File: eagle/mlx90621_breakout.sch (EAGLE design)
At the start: 7 parts, among them J1 ARDUINO_R3_SHIELD

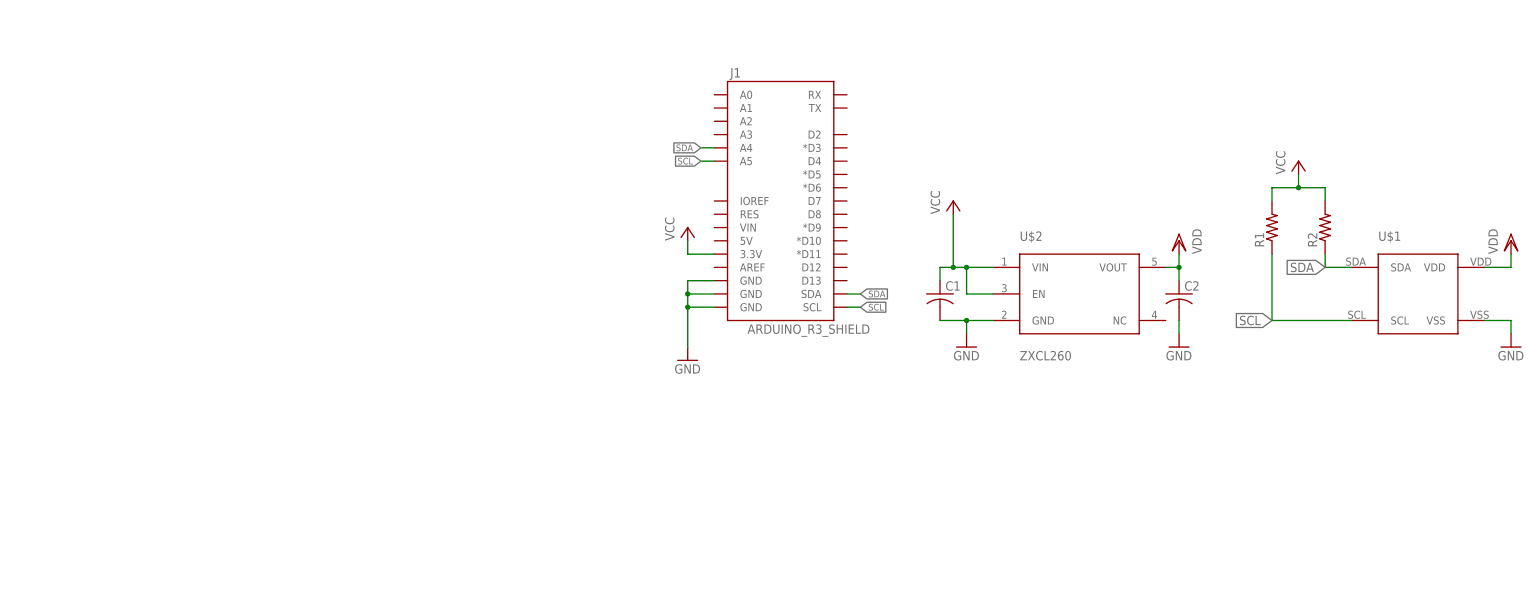
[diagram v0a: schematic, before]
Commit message: Finalizado ruteo de MLX90621 en shield (x1)
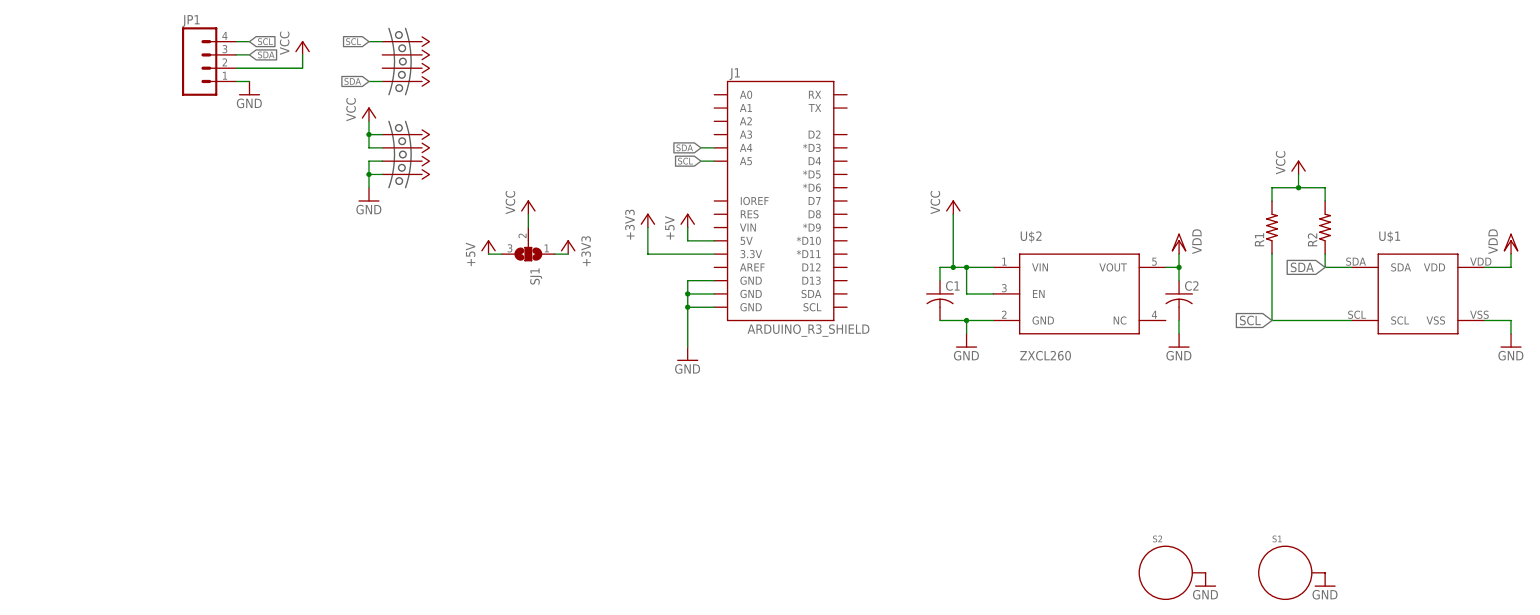
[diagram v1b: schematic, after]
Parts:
- added JP1: (no value), SparkFun-Connectors:M04PTH
- added S1, S2: STANDOFF_ELECTRICAL, SparkFun-Electromechanical:STANDOFF_ELECTRICAL
- added SJ1: (no value), jumper:SJ2W
- added U$3, U$4: MOUSE-BITES-4, mouse-bites:MOUSE-BITES-4
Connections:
- new net +3V3: J1.3.3V, SJ1.1
- new net +5V: J1.5V, SJ1.3
- net GND: now also JP1.1, S1.P$1, S2.P$1, U$4.3, U$4.4
- net SCL: now also JP1.4, U$3.1; no longer J1.SCL
- net SDA: now also JP1.3, U$3.4; no longer J1.SDA
- net VCC: now also JP1.2, SJ1.2, U$4.1, U$4.2; no longer J1.3.3V
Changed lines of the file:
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@@
 <layer number="113" name="IDFDebug" color="7" fill="1" visible="yes" active="yes"/>
 <layer number="114" name="Badge_Outline" color="11" fill="1" visible="no" active="no"/>
+<layer number="115" name="ReferenceISLANDS" color="7" fill="1" visible="yes" active="yes"/>
 <layer number="116" name="Patch_BOT" color="9" fill="4" visible="yes" active="yes"/>
 <layer number="118" name="Rect_Pads" color="7" fill="1" visible="yes" active="yes"/>
@@
 <part name="P+3" library="supply1" deviceset="VCC" device=""/>
 <part name="GND4" library="SparkFun-Aesthetics" deviceset="GND" device=""/>
+<part name="SJ1" library="jumper" deviceset="SJ2W" device=""/>
+<part name="P+4" library="supply1" deviceset="+5V" device=""/>
+<part name="P+5" library="supply1" deviceset="+5V" device=""/>
+<part name="+3V1" library="supply1" deviceset="+3V3" device=""/>
+<part name="+3V2" library="supply1" deviceset="+3V3" device=""/>
+<part name="S1" library="SparkFun-Electromechanical" deviceset="STANDOFF_ELECTRICAL" device=""/>
+<part name="S2" library="SparkFun-Electromechanical" deviceset="STANDOFF_ELECTRICAL" device=""/>
+<part name="GND5" library="SparkFun-Aesthetics" deviceset="GND" device=""/>
+<part name="GND6" library="SparkFun-Aesthetics" deviceset="GND" device=""/>
+<part name="JP1" library="SparkFun-Connectors" deviceset="M04" device="PTH"/>
+<part name="GND7" library="SparkFun-Aesthetics" deviceset="GND" device=""/>
+<part name="P+6" library="supply1" deviceset="VCC" device=""/>
+<part name="U$3" library="mouse-bites" deviceset="MOUSE-BITES-4" device=""/>
+<part name="U$4" library="mouse-bites" deviceset="MOUSE-BITES-4" device=""/>
+<part name="GND8" library="SparkFun-Aesthetics" deviceset="GND" device=""/>
+<part name="P+7" library="supply1" deviceset="VCC" device=""/>
 </parts>
 <sheets>
@@
 <instance part="VDD2" gate="G$1" x="368.3" y="76.2"/>
 <instance part="GND3" gate="1" x="368.3" y="55.88"/>
-<instance part="P+3" gate="VCC" x="210.82" y="78.74"/>
+<instance part="P+3" gate="VCC" x="180.34" y="83.82"/>
 <instance part="GND4" gate="1" x="210.82" y="53.34"/>
+<instance part="SJ1" gate="G$1" x="180.34" y="73.66" rot="R270"/>
+<instance part="P+4" gate="1" x="172.72" y="76.2"/>
+<instance part="P+5" gate="1" x="210.82" y="81.28"/>
+<instance part="+3V1" gate="G$1" x="187.96" y="76.2" rot="MR0"/>
+<instance part="+3V2" gate="G$1" x="203.2" y="81.28"/>
+<instance part="S1" gate="G$1" x="325.12" y="12.7"/>
+<instance part="S2" gate="G$1" x="302.26" y="12.7"/>
+<instance part="GND5" gate="1" x="309.88" y="10.16"/>
+<instance part="GND6" gate="1" x="332.74" y="10.16"/>
+<instance part="JP1" gate="G$1" x="119.38" y="109.22"/>
+<instance part="GND7" gate="1" x="127" y="104.14"/>
+<instance part="P+6" gate="VCC" x="137.16" y="114.3"/>
+<instance part="U$3" gate="G$1" x="152.4" y="116.84"/>
+<instance part="U$4" gate="G$1" x="152.4" y="99.06"/>
+<instance part="GND8" gate="1" x="149.86" y="83.82"/>
+<instance part="P+7" gate="VCC" x="149.86" y="101.6"/>
 </instances>
 <busses>
@@
 <wire x1="210.82" y1="68.58" x2="210.82" y2="66.04" width="0.1524" layer="91"/>
 <junction x="210.82" y="66.04"/>
+</segment>
+<segment>
+<pinref part="S2" gate="G$1" pin="P$1"/>
+<pinref part="GND5" gate="1" pin="GND"/>
+</segment>
+<segment>
+<pinref part="S1" gate="G$1" pin="P$1"/>
+<pinref part="GND6" gate="1" pin="GND"/>
+</segment>
+<segment>
+<pinref part="JP1" gate="G$1" pin="1"/>
+<wire x1="124.46" y1="106.68" x2="127" y2="106.68" width="0.1524" layer="91"/>
+<pinref part="GND7" gate="1" pin="GND"/>
+</segment>
+<segment>
+<pinref part="U$4" gate="G$1" pin="3"/>
+<wire x1="152.4" y1="91.44" x2="149.86" y2="91.44" width="0.1524" layer="91"/>
+<pinref part="U$4" gate="G$1" pin="4"/>
+<wire x1="152.4" y1="88.9" x2="149.86" y2="88.9" width="0.1524" layer="91"/>
+<wire x1="149.86" y1="91.44" x2="149.86" y2="88.9" width="0.1524" layer="91"/>
+<pinref part="GND8" gate="1" pin="GND"/>
+<wire x1="149.86" y1="88.9" x2="149.86" y2="86.36" width="0.1524" layer="91"/>
+<junction x="149.86" y="88.9"/>
 </segment>
 </net>
@@
 </segment>
 <segment>
-<pinref part="J1" gate="G$1" pin="3.3V"/>
+<pinref part="SJ1" gate="G$1" pin="2"/>
 <pinref part="P+3" gate="VCC" pin="VCC"/>
-<wire x1="215.9" y1="73.66" x2="210.82" y2="73.66" width="0.1524" layer="91"/>
-<wire x1="210.82" y1="73.66" x2="210.82" y2="76.2" width="0.1524" layer="91"/>
+<wire x1="180.34" y1="81.28" x2="180.34" y2="78.74" width="0.1524" layer="91"/>
+</segment>
+<segment>
+<pinref part="JP1" gate="G$1" pin="2"/>
+<wire x1="124.46" y1="109.22" x2="137.16" y2="109.22" width="0.1524" layer="91"/>
+<wire x1="137.16" y1="109.22" x2="137.16" y2="111.76" width="0.1524" layer="91"/>
+<pinref part="P+6" gate="VCC" pin="VCC"/>
+</segment>
+<segment>
+<pinref part="U$4" gate="G$1" pin="2"/>
+<wire x1="152.4" y1="93.98" x2="149.86" y2="93.98" width="0.1524" layer="91"/>
+<pinref part="U$4" gate="G$1" pin="1"/>
+<wire x1="152.4" y1="96.52" x2="149.86" y2="96.52" width="0.1524" layer="91"/>
+<wire x1="149.86" y1="93.98" x2="149.86" y2="96.52" width="0.1524" layer="91"/>
+<pinref part="P+7" gate="VCC" pin="VCC"/>
+<wire x1="149.86" y1="96.52" x2="149.86" y2="99.06" width="0.1524" layer="91"/>
+<junction x="149.86" y="96.52"/>
 </segment>
 </net>
@@
 </segment>
 <segment>
-<pinref part="J1" gate="G$1" pin="SDA"/>
-<wire x1="241.3" y1="66.04" x2="243.84" y2="66.04" width="0.1524" layer="91"/>
-<label x="243.84" y="66.04" size="1.27" layer="95" xref="yes"/>
-</segment>
-<segment>
 <pinref part="J1" gate="G$1" pin="A4"/>
 <wire x1="215.9" y1="93.98" x2="213.36" y2="93.98" width="0.1524" layer="91"/>
 <label x="213.36" y="93.98" size="1.27" layer="95" rot="R180" xref="yes"/>
+</segment>
+<segment>
+<pinref part="JP1" gate="G$1" pin="3"/>
+<wire x1="124.46" y1="111.76" x2="127" y2="111.76" width="0.1524" layer="91"/>
+<label x="127" y="111.76" size="1.27" layer="95" xref="yes"/>
+</segment>
+<segment>
+<pinref part="U$3" gate="G$1" pin="4"/>
+<wire x1="152.4" y1="106.68" x2="149.86" y2="106.68" width="0.1524" layer="91"/>
+<label x="149.86" y="106.68" size="1.27" layer="95" rot="R180" xref="yes"/>
 </segment>
 </net>
@@
 </segment>
 <segment>
-<pinref part="J1" gate="G$1" pin="SCL"/>
-<wire x1="241.3" y1="63.5" x2="243.84" y2="63.5" width="0.1524" layer="91"/>
-<label x="243.84" y="63.5" size="1.27" layer="95" xref="yes"/>
-</segment>
-<segment>
 <pinref part="J1" gate="G$1" pin="A5"/>
 <wire x1="215.9" y1="91.44" x2="213.36" y2="91.44" width="0.1524" layer="91"/>
 <label x="213.36" y="91.44" size="1.27" layer="95" rot="R180" xref="yes"/>
 </segment>
-</net>
+<segment>
+<pinref part="JP1" gate="G$1" pin="4"/>
+<wire x1="124.46" y1="114.3" x2="127" y2="114.3" width="0.1524" layer="91"/>
+<label x="127" y="114.3" size="1.27" layer="95" xref="yes"/>
+</segment>
+<segment>
+<pinref part="U$3" gate="G$1" pin="1"/>
+<wire x1="152.4" y1="114.3" x2="149.86" y2="114.3" width="0.1524" layer="91"/>
+<label x="149.86" y="114.3" size="1.27" layer="95" rot="R180" xref="yes"/>
+</segment>
+</net>
+<net name="+3V3" class="0">
+<segment>
+<pinref part="J1" gate="G$1" pin="3.3V"/>
+<pinref part="+3V2" gate="G$1" pin="+3V3"/>
+<wire x1="203.2" y1="78.74" x2="203.2" y2="73.66" width="0.1524" layer="91"/>
+<wire x1="203.2" y1="73.66" x2="215.9" y2="73.66" width="0.1524" layer="91"/>
+</segment>
+<segment>
+<pinref part="SJ1" gate="G$1" pin="1"/>
+<pinref part="+3V1" gate="G$1" pin="+3V3"/>
+<wire x1="187.96" y1="73.66" x2="185.42" y2="73.66" width="0.1524" layer="91"/>
+</segment>
+</net>
+<net name="+5V" class="0">
+<segment>
+<pinref part="SJ1" gate="G$1" pin="3"/>
+<pinref part="P+4" gate="1" pin="+5V"/>
+<wire x1="172.72" y1="73.66" x2="175.26" y2="73.66" width="0.1524" layer="91"/>
+</segment>
+<segment>
+<pinref part="J1" gate="G$1" pin="5V"/>
+<pinref part="P+5" gate="1" pin="+5V"/>
+<wire x1="210.82" y1="78.74" x2="210.82" y2="76.2" width="0.1524" layer="91"/>
+<wire x1="210.82" y1="76.2" x2="215.9" y2="76.2" width="0.1524" layer="91"/>
+</segment>
+</net>

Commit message: Finalizado diseño de panel shield
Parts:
- added U$5, U$6, U$7: MOUSE-BITES-4, mouse-bites:MOUSE-BITES-4
- C1, C2: value (none) -> 100n
- R1, R2: value (none) -> 10k
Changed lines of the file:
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@@
 <part name="J1" library="SparkFun-Boards" deviceset="ARDUINO_R3_SHIELD" device=""/>
 <part name="FRAME1" library="frames" deviceset="A3L-LOC" device=""/>
-<part name="C1" library="adafruit" deviceset="C-US" device="C0603"/>
-<part name="C2" library="adafruit" deviceset="C-US" device="C0603"/>
-<part name="R1" library="adafruit" deviceset="R-US_" device="R0603"/>
-<part name="R2" library="adafruit" deviceset="R-US_" device="R0603"/>
+<part name="C1" library="adafruit" deviceset="C-US" device="C0603" value="100n"/>
+<part name="C2" library="adafruit" deviceset="C-US" device="C0603" value="100n"/>
+<part name="R1" library="adafruit" deviceset="R-US_" device="R0603" value="10k"/>
+<part name="R2" library="adafruit" deviceset="R-US_" device="R0603" value="10k"/>
 <part name="U$1" library="melexis" deviceset="MLX90621" device="BAD"/>
 <part name="U$2" library="melexis" deviceset="ZXCL260" device=""/>
@@
 <part name="GND8" library="SparkFun-Aesthetics" deviceset="GND" device=""/>
 <part name="P+7" library="supply1" deviceset="VCC" device=""/>
+<part name="U$5" library="mouse-bites" deviceset="MOUSE-BITES-4" device=""/>
+<part name="U$6" library="mouse-bites" deviceset="MOUSE-BITES-4" device=""/>
+<part name="U$7" library="mouse-bites" deviceset="MOUSE-BITES-4" device=""/>
 </parts>
 <sheets>
@@
 <instance part="GND8" gate="1" x="149.86" y="83.82"/>
 <instance part="P+7" gate="VCC" x="149.86" y="101.6"/>
+<instance part="U$5" gate="G$1" x="81.28" y="43.18"/>
+<instance part="U$6" gate="G$1" x="81.28" y="25.4"/>
+<instance part="U$7" gate="G$1" x="99.06" y="25.4"/>
 </instances>
 <busses>
